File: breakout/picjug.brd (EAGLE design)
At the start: 44.5 x 31.8 mm, 38 parts, among them Q1 BSS138, Q2 BSS138, Q3 BSS84, Q4 BSS84, U1 PIC16F1454SOIC, U2 AP7115W, X1 MINI-USB-UX60-MB-5ST

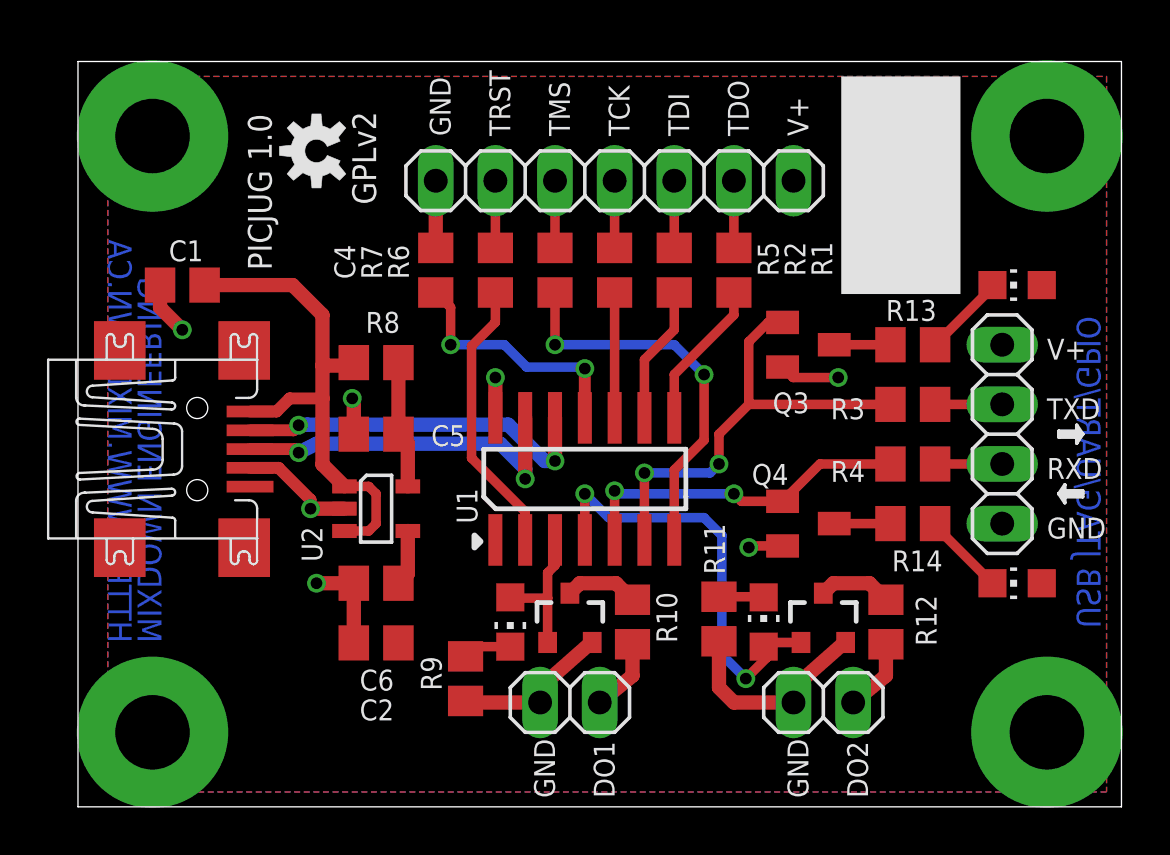
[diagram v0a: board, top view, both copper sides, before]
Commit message: add test points for in system programming
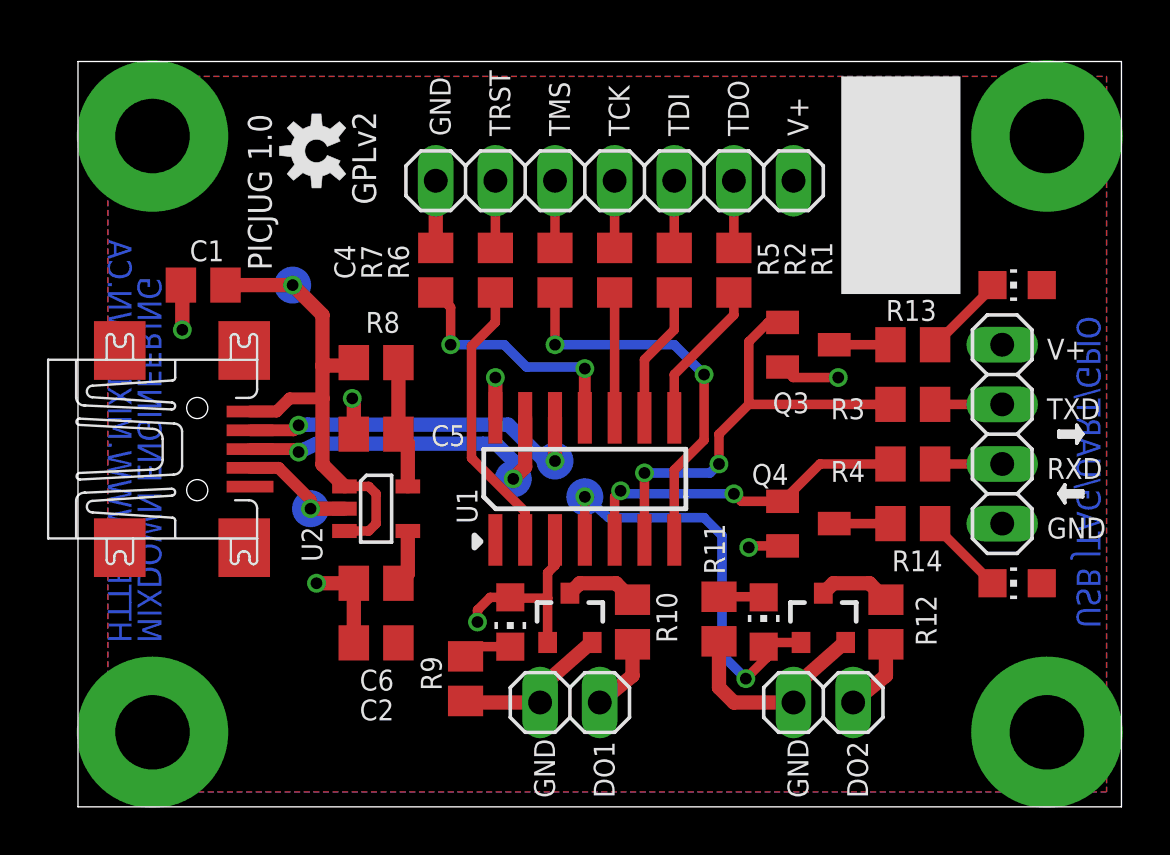
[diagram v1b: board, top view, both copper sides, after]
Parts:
- added GND, ICSPCLK, ICSPDAT, VPP, VUSB: TESTPOINTMILLMAX_0900_SMALL, ak-misc:0900-SERIES-SM
- moved C1 0.89 mm to (5.33, 22.2)
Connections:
- net DO2: now also VPP.P$1
- net D_N: now also ICSPDAT.P$1
- net D_P: now also ICSPCLK.P$1
- net GND: now also GND.P$1
- net VUSB: now also VUSB.P$1
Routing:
- net DO1: track 6.12 -> 8.25 mm, vias 0 -> 1
- net VUSB: track 22.2 -> 21.3 mm, vias 0 -> 1
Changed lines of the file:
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@@
 <setting verticaltext="up"/>
 </settings>
-<grid distance="5" unitdist="mil" unit="mil" style="lines" multiple="1" display="yes" altdistance="0.025" altunitdist="inch" altunit="inch"/>
+<grid distance="25" unitdist="mil" unit="mil" style="lines" multiple="1" display="yes" altdistance="0.025" altunitdist="inch" altunit="inch"/>
 <layers>
 <layer number="1" name="Top" color="4" fill="1" visible="yes" active="yes"/>
@@
 <layer number="21" name="tPlace" color="7" fill="1" visible="yes" active="yes"/>
 <layer number="22" name="bPlace" color="7" fill="1" visible="no" active="yes"/>
-<layer number="23" name="tOrigins" color="15" fill="1" visible="yes" active="yes"/>
-<layer number="24" name="bOrigins" color="15" fill="1" visible="no" active="yes"/>
+<layer number="23" name="tOrigins" color="15" fill="1" visible="no" active="yes"/>
+<layer number="24" name="bOrigins" color="15" fill="1" visible="yes" active="yes"/>
 <layer number="25" name="tNames" color="7" fill="1" visible="yes" active="yes"/>
 <layer number="26" name="bNames" color="7" fill="1" visible="no" active="yes"/>
@@
 <attribute name="VALUE" x="36.195" y="20.955" size="1.27" layer="27" rot="R270"/>
 </element>
-<element name="C1" library="rcl" package="C0805" value="1" x="4.445" y="22.225" smashed="yes" rot="R180">
-<attribute name="NAME" x="5.334" y="24.13" size="0.889" layer="25" ratio="15" rot="R180"/>
-<attribute name="VALUE" x="5.715" y="24.765" size="1.27" layer="27" rot="R180"/>
+<element name="C1" library="rcl" package="C0805" value="1" x="5.334" y="22.225" smashed="yes" rot="R180">
+<attribute name="NAME" x="6.223" y="24.13" size="0.889" layer="25" ratio="15" rot="R180"/>
+<attribute name="VALUE" x="6.604" y="24.765" size="1.27" layer="27" rot="R180"/>
 </element>
 <element name="C2" library="rcl" package="C0805" value="0.1" x="12.7" y="6.985" smashed="yes" rot="R180">
@@
 <element name="LED3" library="led" package="CHIP-LED0805" value="" x="40.005" y="22.225" smashed="yes" rot="R90">
 <attribute name="VALUE" x="41.275" y="24.765" size="1.27" layer="27" rot="R180"/>
+</element>
+<element name="ICSPDAT" library="ak-misc" package="0900-SERIES-SM" value="TESTPOINTMILLMAX_0900_SMALL" x="20.32" y="14.732" locked="yes" smashed="yes" rot="MR0">
+<attribute name="NAME" x="19.05" y="15.367" size="0.889" layer="26" ratio="15" rot="MR0"/>
+</element>
+<element name="ICSPCLK" library="ak-misc" package="0900-SERIES-SM" value="TESTPOINTMILLMAX_0900_SMALL" x="18.542" y="13.97" locked="yes" smashed="yes" rot="MR0">
+<attribute name="NAME" x="17.272" y="13.335" size="0.889" layer="26" ratio="15" rot="MR0"/>
+</element>
+<element name="VPP" library="ak-misc" package="0900-SERIES-SM" value="TESTPOINTMILLMAX_0900_SMALL" x="21.59" y="13.208" locked="yes" smashed="yes" rot="MR0">
+<attribute name="NAME" x="22.225" y="10.668" size="0.889" layer="26" ratio="15" rot="MR0"/>
+</element>
+<element name="VUSB" library="ak-misc" package="0900-SERIES-SM" value="TESTPOINTMILLMAX_0900_SMALL" x="9.144" y="22.225" locked="yes" smashed="yes" rot="MR0">
+<attribute name="NAME" x="10.414" y="19.685" size="0.889" layer="26" ratio="15" rot="MR0"/>
+</element>
+<element name="GND" library="ak-misc" package="0900-SERIES-SM" value="TESTPOINTMILLMAX_0900_SMALL" x="9.906" y="12.7" smashed="yes" rot="MR0">
+<attribute name="NAME" x="11.176" y="10.16" size="0.889" layer="26" ratio="15" rot="MR0"/>
 </element>
 </elements>
@@
 <wire x1="8.547" y1="14.44" x2="9.906" y2="13.081" width="0.508" layer="1"/>
 <wire x1="9.906" y1="13.081" x2="9.906" y2="12.7" width="0.508" layer="1"/>
-<wire x1="3.495" y1="22.225" x2="3.495" y2="21.27" width="0.6096" layer="1"/>
-<wire x1="3.495" y1="21.27" x2="4.445" y2="20.32" width="0.6096" layer="1"/>
+<wire x1="4.384" y1="22.225" x2="4.445" y2="22.225" width="0.6096" layer="1"/>
+<wire x1="4.445" y1="22.225" x2="4.445" y2="20.32" width="0.6096" layer="1"/>
+<contactref element="GND" pad="P$1"/>
 </signal>
 <signal name="D_N">
@@
 <wire x1="18.3293375" y1="16.2814" x2="19.8787375" y2="14.732" width="0.6096" layer="16"/>
 <wire x1="19.8787375" y1="14.732" x2="20.32" y2="14.732" width="0.6096" layer="16"/>
+<contactref element="ICSPDAT" pad="P$1"/>
 </signal>
 <signal name="D_P">
 <contactref element="X1" pad="3"/>
 <contactref element="U1" pad="13"/>
-<via x="9.398" y="15.0876" extent="1-16" drill="0.5"/>
-<via x="19.05" y="13.97" extent="1-16" drill="0.5"/>
+<via x="9.398" y="15.113" extent="1-16" drill="0.5"/>
+<via x="18.542" y="13.97" extent="1-16" drill="0.5"/>
 <wire x1="7.33" y1="15.24" x2="9.271" y2="15.24" width="0.508" layer="1"/>
-<wire x1="9.271" y1="15.24" x2="9.398" y2="15.0876" width="0.508" layer="1"/>
-<wire x1="9.398" y1="15.0876" x2="10.16" y2="15.4686" width="0.6096" layer="16"/>
-<wire x1="10.16" y1="15.4686" x2="17.9926625" y2="15.4686" width="0.6096" layer="16"/>
-<wire x1="17.9926625" y1="15.4686" x2="19.05" y2="14.4112625" width="0.6096" layer="16"/>
-<wire x1="19.05" y1="14.4112625" x2="19.05" y2="13.97" width="0.6096" layer="16"/>
-<wire x1="19.05" y1="16.57" x2="19.05" y2="13.97" width="0.6096" layer="1"/>
+<wire x1="9.271" y1="15.24" x2="9.398" y2="15.113" width="0.508" layer="1"/>
+<wire x1="9.398" y1="15.113" x2="10.16" y2="15.4686" width="0.6096" layer="16"/>
+<wire x1="10.16" y1="15.4686" x2="17.2306625" y2="15.4686" width="0.6096" layer="16"/>
+<wire x1="19.05" y1="16.57" x2="19.05" y2="14.478" width="0.6096" layer="1"/>
+<wire x1="19.05" y1="14.478" x2="18.542" y2="13.97" width="0.6096" layer="1"/>
+<contactref element="ICSPCLK" pad="P$1"/>
+<wire x1="17.2466" y1="15.4686" x2="17.272" y2="15.494" width="0.1524" layer="16"/>
+<wire x1="17.2466" y1="15.4686" x2="17.8054" y2="15.4686" width="0.6096" layer="16"/>
+<wire x1="17.8054" y1="15.4686" x2="18.542" y2="14.732" width="0.6096" layer="16"/>
+<wire x1="18.542" y1="14.732" x2="18.542" y2="13.97" width="0.6096" layer="16"/>
+<wire x1="17.2306625" y1="15.4686" x2="17.2466" y2="15.4686" width="0" layer="19" extent="16-16"/>
 </signal>
 <signal name="N$5">
@@
 <contactref element="R4" pad="1"/>
 <contactref element="U1" pad="5"/>
-<wire x1="22.86" y1="11.37" x2="22.86" y2="13.462" width="0.4064" layer="1"/>
-<via x="22.86" y="13.462" extent="1-16" drill="0.5"/>
+<via x="23.114" y="13.462" extent="1-16" drill="0.5"/>
 <via x="27.94" y="13.335" extent="1-16" drill="0.5"/>
-<wire x1="22.86" y1="13.462" x2="22.987" y2="13.335" width="0.4064" layer="16"/>
+<wire x1="23.114" y1="13.462" x2="22.987" y2="13.335" width="0.4064" layer="16"/>
 <wire x1="22.987" y1="13.335" x2="27.94" y2="13.335" width="0.4064" layer="16"/>
 <contactref element="Q4" pad="1"/>
@@
 <wire x1="27.94" y1="13.335" x2="28.26" y2="13.015" width="0.4064" layer="1"/>
 <wire x1="28.26" y1="13.015" x2="30.015" y2="13.015" width="0.4064" layer="1"/>
+<wire x1="22.86" y1="11.37" x2="22.86" y2="13.208" width="0.4064" layer="1"/>
+<wire x1="22.86" y1="13.208" x2="23.114" y2="13.462" width="0.4064" layer="1"/>
 </signal>
 <signal name="N$3">
@@
 <wire x1="12.7" y1="13.335" x2="12.385" y2="13.65" width="0.4064" layer="1"/>
 <wire x1="12.385" y1="13.65" x2="11.35" y2="13.65" width="0.4064" layer="1"/>
-<wire x1="5.395" y1="22.225" x2="9.144" y2="22.225" width="0.6096" layer="1"/>
+<wire x1="6.284" y1="22.225" x2="9.144" y2="22.225" width="0.6096" layer="1"/>
 <wire x1="9.144" y1="22.225" x2="10.414" y2="20.955" width="0.6096" layer="1"/>
 <wire x1="10.414" y1="20.955" x2="10.414" y2="18.796" width="0.6096" layer="1"/>
@@
 <wire x1="8.458" y1="16.84" x2="9.017" y2="17.399" width="0.508" layer="1"/>
 <wire x1="9.017" y1="17.399" x2="10.414" y2="17.399" width="0.508" layer="1"/>
+<via x="9.144" y="22.225" extent="1-16" drill="0.5"/>
+<contactref element="VUSB" pad="P$1"/>
 </signal>
 <signal name="N$2">
@@
 <wire x1="18.415" y1="8.924" x2="18.681" y2="8.924" width="0.4064" layer="1"/>
 <wire x1="18.681" y1="8.924" x2="18.681" y2="8.89" width="0.4064" layer="1"/>
+<via x="17.018" y="7.874" extent="1-16" drill="0.5"/>
+<wire x1="18.415" y1="8.924" x2="17.56" y2="8.924" width="0.4064" layer="1"/>
+<wire x1="17.56" y1="8.924" x2="17.018" y2="8.382" width="0.4064" layer="1"/>
+<wire x1="17.018" y1="8.382" x2="17.018" y2="7.874" width="0.4064" layer="1"/>
 </signal>
 <signal name="N$8">
@@
 <contactref element="U1" pad="4"/>
 <wire x1="29.718" y1="7.001" x2="29.333" y2="7.001" width="0.4064" layer="1"/>
-<wire x1="21.59" y1="11.37" x2="21.59" y2="13.335" width="0.4064" layer="1"/>
-<via x="21.59" y="13.335" extent="1-16" drill="0.5"/>
+<wire x1="21.59" y1="11.37" x2="21.59" y2="13.208" width="0.4064" layer="1"/>
+<via x="21.59" y="13.208" extent="1-16" drill="0.5"/>
 <via x="28.448" y="5.461" extent="1-16" drill="0.5"/>
-<wire x1="21.59" y1="13.335" x2="22.606" y2="12.319" width="0.4064" layer="16"/>
+<wire x1="21.59" y1="13.208" x2="22.606" y2="12.319" width="0.4064" layer="16"/>
 <contactref element="LED2" pad="A"/>
 <wire x1="29.21" y1="6.824" x2="29.541" y2="6.824" width="0.4064" layer="1"/>
@@
 <wire x1="27.432" y1="11.557" x2="27.432" y2="6.477" width="0.4064" layer="16"/>
 <wire x1="27.432" y1="6.477" x2="28.448" y2="5.461" width="0.4064" layer="16"/>
+<contactref element="VPP" pad="P$1"/>
 </signal>
 <signal name="N$17">

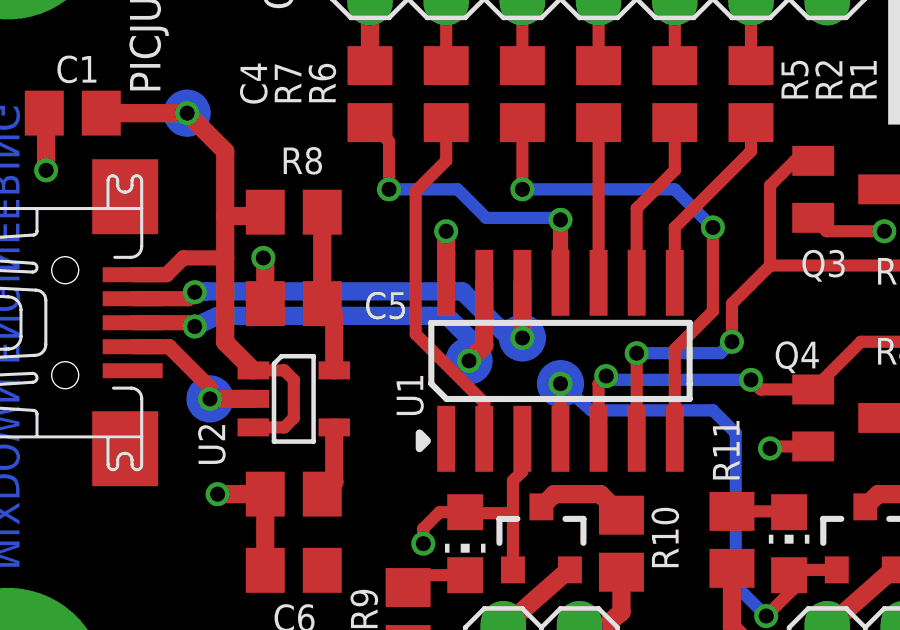
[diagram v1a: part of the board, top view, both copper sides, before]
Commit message: fix spacing violation, re-do copper pours with 10mil lines and 24mil isolation
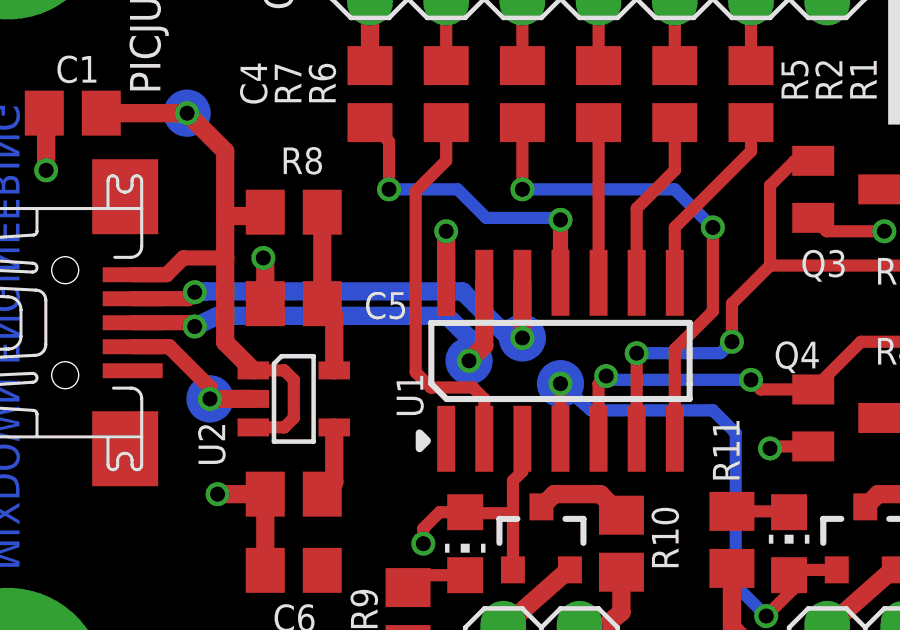
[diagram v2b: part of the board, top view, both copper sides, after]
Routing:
- net TRST: track 11.9 -> 12.7 mm
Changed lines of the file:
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@@
 <setting verticaltext="up"/>
 </settings>
-<grid distance="25" unitdist="mil" unit="mil" style="lines" multiple="1" display="yes" altdistance="0.025" altunitdist="inch" altunit="inch"/>
+<grid distance="5" unitdist="mil" unit="mil" style="lines" multiple="1" display="yes" altdistance="0.025" altunitdist="inch" altunit="inch"/>
 <layers>
 <layer number="1" name="Top" color="4" fill="1" visible="yes" active="yes"/>
@@
 <wire x1="11.75" y1="15.875" x2="11.75" y2="17.333" width="0.6096" layer="1"/>
 <wire x1="11.75" y1="17.333" x2="11.684" y2="17.399" width="0.6096" layer="1"/>
-<polygon width="0.6096" layer="16" isolate="0.4064">
+<polygon width="0.254" layer="16" isolate="0.6096">
 <vertex x="1.27" y="0.635"/>
 <vertex x="1.27" y="31.115"/>
@@
 <contactref element="R7" pad="1"/>
 <contactref element="U1" pad="2"/>
-<wire x1="16.764" y1="19.624" x2="16.764" y2="14.859" width="0.4064" layer="1"/>
-<wire x1="16.764" y1="14.859" x2="19.05" y2="12.573" width="0.4064" layer="1"/>
-<wire x1="19.05" y1="12.573" x2="19.05" y2="11.37" width="0.4064" layer="1"/>
+<wire x1="16.764" y1="19.624" x2="16.764" y2="13.589" width="0.4064" layer="1"/>
+<wire x1="19.05" y1="12.7" x2="19.05" y2="11.37" width="0.4064" layer="1"/>
 <wire x1="16.764" y1="19.624" x2="17.78" y2="20.64" width="0.4064" layer="1"/>
 <wire x1="17.78" y1="20.64" x2="17.78" y2="21.91" width="0.4064" layer="1"/>
+<wire x1="19.05" y1="12.7" x2="18.669" y2="13.081" width="0.4064" layer="1"/>
+<wire x1="18.669" y1="13.081" x2="17.272" y2="13.081" width="0.4064" layer="1"/>
+<wire x1="17.272" y1="13.081" x2="16.764" y2="13.589" width="0.4064" layer="1"/>
 </signal>
 <signal name="N$1">
@@
 <wire x1="14.05" y1="15.475" x2="13.65" y2="15.875" width="0.6096" layer="1"/>
 <wire x1="13.65" y1="15.875" x2="13.65" y2="18.923" width="0.6096" layer="1"/>
-<polygon width="0.6096" layer="1" isolate="0.4064">
+<polygon width="0.254" layer="1" isolate="0.6096">
 <vertex x="1.27" y="0.635"/>
 <vertex x="1.27" y="31.115"/>
